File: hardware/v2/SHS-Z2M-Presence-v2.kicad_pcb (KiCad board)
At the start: 2 copper layers, 100 x 70 mm, 36 parts, among them J1 USB_C_Receptacle, SW1 RESET, SW2 BOOT, U1 ESP32-C6-WROOM-1-N8, U2 LD2410C, U3 LD2450, U4 AP2112K-3.3

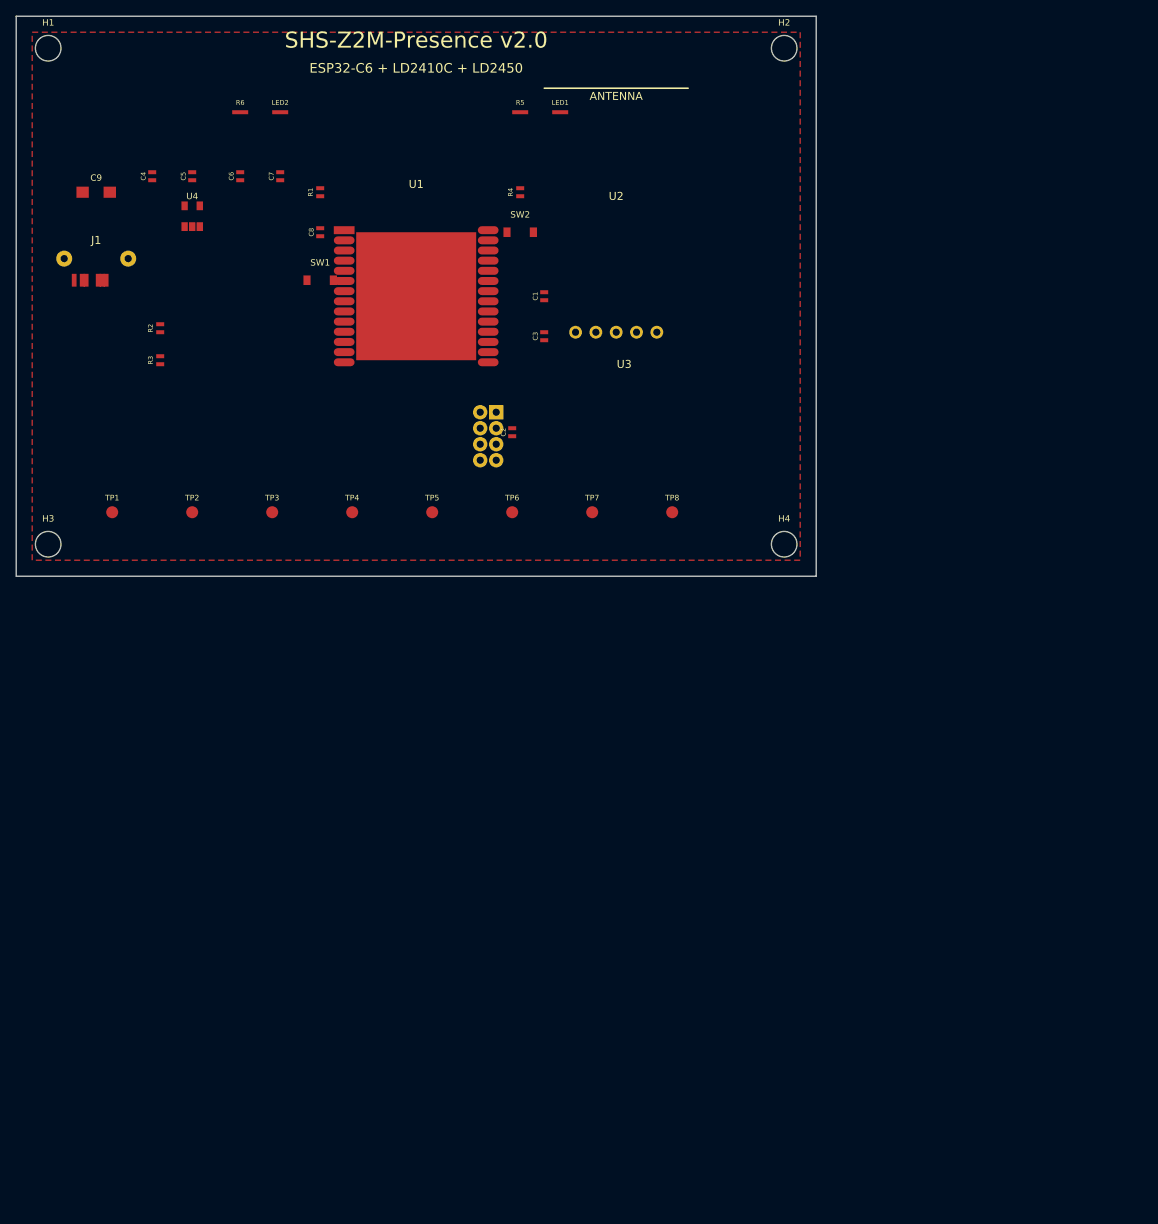
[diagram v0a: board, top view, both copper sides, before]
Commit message: Rewrite v2 PCB layout: compact 39x49mm 4-layer board
- Board outline reduced from 100x70mm to 39x49mm (73% area reduction)
- 4-layer stackup: F.Cu (sensors), In1.Cu (GND plane), In2.Cu (+3V3), B.Cu (SMD)
- Sensors (LD2410C, LD2450) placed on F.Cu with THT headers
- All SMD components (ESP32, LDO, USB-C, passives) on B.Cu
- GND zones on F.Cu, In1.Cu, B.Cu; +3V3 power plane on In2.Cu
- Fiducials at 3 corners for SMD assembly
- Update DESIGN-NOTES.md with 4-layer decision and board dimensions
- Add .history/ to .gitignore (KiCad local undo history)

Co-Authored-By: Claude Opus 4.6 <noreply@anthropic.com>
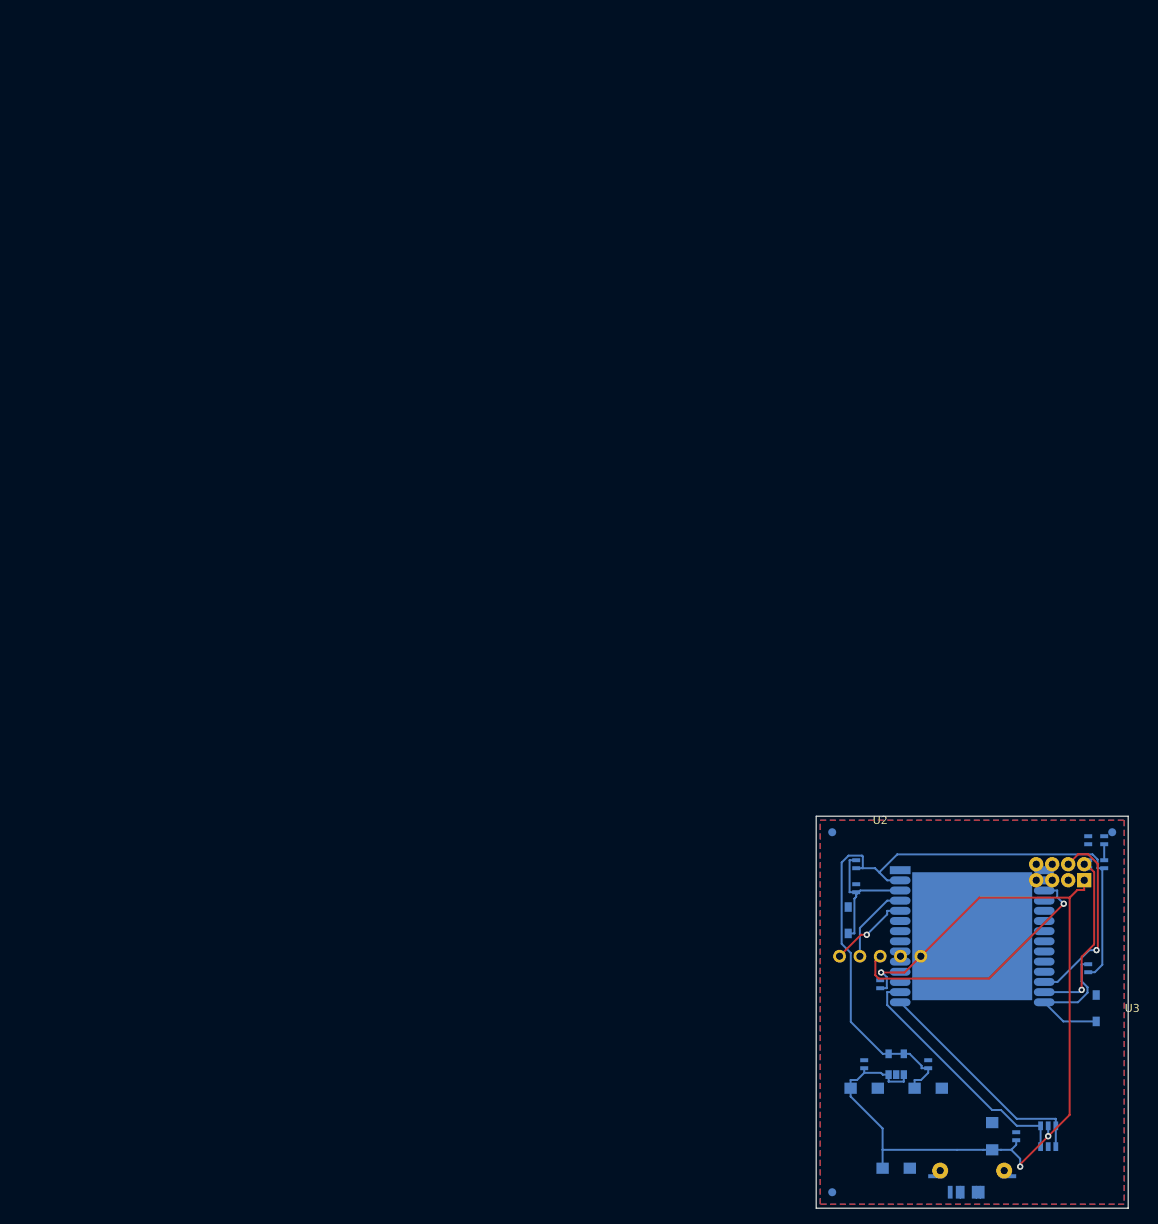
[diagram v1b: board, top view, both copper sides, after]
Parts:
- removed H1, H2, H3, H4: M3, MountingHole:MountingHole_3.2mm_M3
- removed TP1: +5V, TestPoint:TestPoint_Pad_D1.5mm
- removed TP2: +3V3, TestPoint:TestPoint_Pad_D1.5mm
- removed TP3: GND, TestPoint:TestPoint_Pad_D1.5mm
- removed TP4: UART1_TX, TestPoint:TestPoint_Pad_D1.5mm
- removed TP5: UART1_RX, TestPoint:TestPoint_Pad_D1.5mm
- removed TP6: UART0_TX, TestPoint:TestPoint_Pad_D1.5mm
- removed TP7: UART0_RX, TestPoint:TestPoint_Pad_D1.5mm
- removed TP8: ESP_EN, TestPoint:TestPoint_Pad_D1.5mm
- added FID1: Fiducial, Fiducial:Fiducial_1mm_Dia_2mm_Outer, B.Cu at (102.0, 102.0)
- added FID2: Fiducial, Fiducial:Fiducial_1mm_Dia_2mm_Outer, B.Cu at (137.0, 102.0)
- added FID3: Fiducial, Fiducial:Fiducial_1mm_Dia_2mm_Outer, B.Cu at (102.0, 147.0)
- added U5: USBLC6-2SC6, Package_TO_SOT_SMD:SOT-23-6, B.Cu at (129.0, 140.0)
- C1, C2, C4, C6, C8, C9, J1, LED1, LED2, R1, R2, R3, R4, R5, R6, SW1, SW2, U1, U4: moved to B.Cu
- C3, C5, C7: footprint Capacitor_SMD:C_0402_1005Metric -> Capacitor_SMD:C_0805_2012Metric; moved to B.Cu
- moved J1 158.1 mm to (119.5, 147.0)
- moved C9 157.7 mm to (110.0, 144.0)
- moved R3 147.1 mm to (124.0, 145.0), turned to 0 degrees
- moved R2 143.7 mm to (115.0, 145.0), turned to 0 degrees
- moved R6 143.2 mm to (136.0, 106.0), turned to 90 degrees
- moved C4 142.3 mm to (106.0, 131.0)
- moved C5 141.6 mm to (106.0, 134.0), turned to 0 degrees
- moved C6 140.4 mm to (114.0, 131.0)
- moved C7 139.8 mm to (114.0, 134.0), turned to 0 degrees
- moved U4 137.8 mm to (110.0, 131.0)
- moved LED2 137.4 mm to (136.0, 103.0), turned to 90 degrees
- moved SW2 120.8 mm to (135.0, 124.0), turned to 90 degrees
- moved R4 120.2 mm to (134.0, 119.0)
- moved R5 117.8 mm to (134.0, 106.0), turned to 90 degrees
- moved C3 114.6 mm to (122.0, 140.0)
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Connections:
- LED1 pad 1: GND -> Net-R5-A
- LED1 pad 2: Net-R5-A -> GND
- LED2 pad 1: GND -> Net-R6-A
- LED2 pad 2: Net-R6-A -> GND
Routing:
- net +5V: track 0.00 -> 113.7 mm, vias 0 -> 3
- net +3V3: track 0.00 -> 91.7 mm
- net RADAR_OUT: track 0.00 -> 33.8 mm, vias 0 -> 1
- net USB_DM: track 0.00 -> 31.3 mm
- net USB_DP: track 0.00 -> 29.0 mm
- net UART0_RX: track 0.00 -> 23.8 mm, vias 0 -> 1
- net UART0_TX: track 0.00 -> 21.8 mm, vias 0 -> 1
- net BOOT: track 0.00 -> 18.1 mm
- net ESP_EN: track 0.00 -> 17.4 mm
- net UART1_RX: track 0.00 -> 10.2 mm, vias 0 -> 1
- net UART1_TX: track 0.00 -> 9.99 mm
- net Net-R6-A: track 0.00 -> 2.00 mm
- added copper zone on In2.Cu, net +3V3
- added copper zone on B.Cu, net GND
- added copper zone on In1.Cu, net GND
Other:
- board size 100 x 70 mm -> 39 x 49 mm
- copper layers 2 -> 4
- board text added: "SHS-Z2M-Presence v2"
- board text removed: "ANTENNA"
- board text removed: "ESP32-C6 + LD2410C + LD2450"
- board text removed: "SHS-Z2M-Presence v2.0"

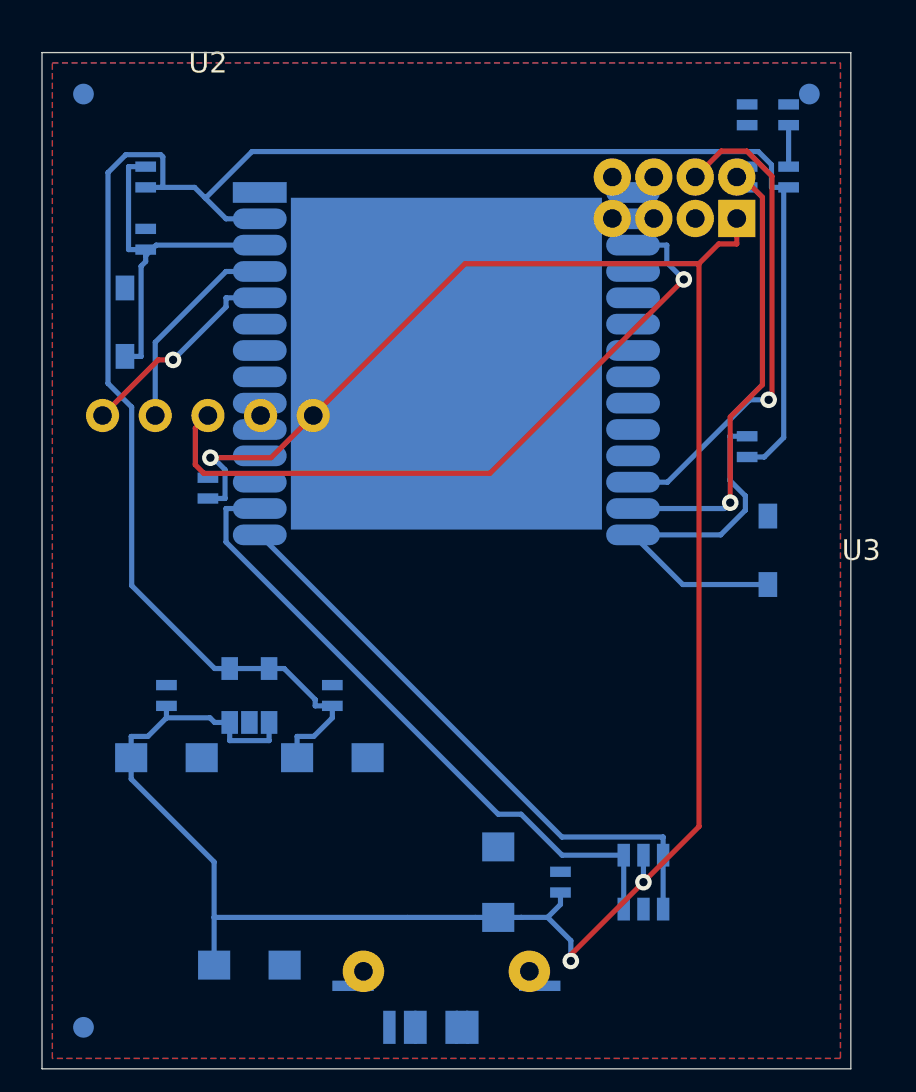
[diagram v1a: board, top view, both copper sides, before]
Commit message: Remove all tracks from v2 PCB for clean rerouting
Strip 134 auto-generated segments — board is now unrouted
and ready for interactive routing in KiCad.

Co-Authored-By: Claude Opus 4.6 <noreply@anthropic.com>
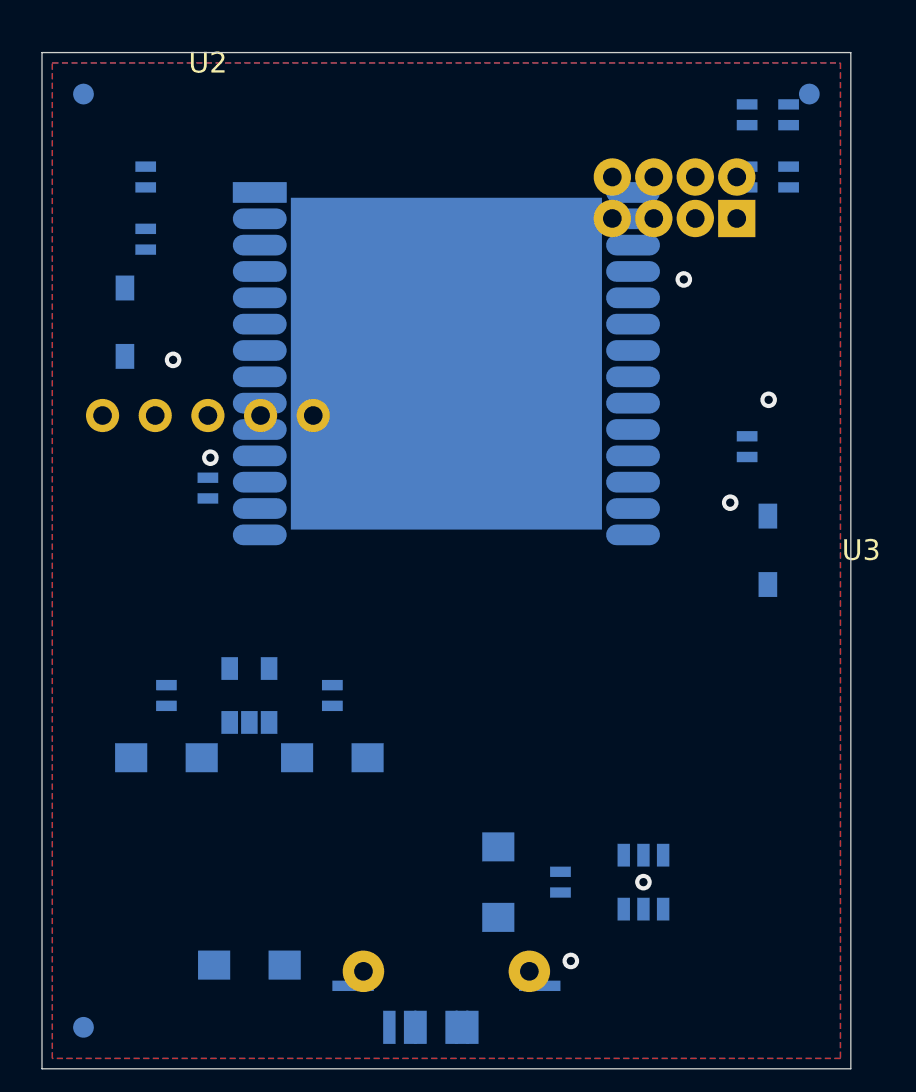
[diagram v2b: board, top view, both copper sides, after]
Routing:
- net +5V: track 113.7 -> 0.00 mm
- net +3V3: track 91.7 -> 0.00 mm
- net RADAR_OUT: track 33.8 -> 0.00 mm
- net USB_DM: track 31.3 -> 0.00 mm
- net USB_DP: track 29.0 -> 0.00 mm
- net UART0_RX: track 23.8 -> 0.00 mm
- net UART0_TX: track 21.8 -> 0.00 mm
- net BOOT: track 18.1 -> 0.00 mm
- net ESP_EN: track 17.4 -> 0.00 mm
- net UART1_RX: track 10.2 -> 0.00 mm
- net UART1_TX: track 9.99 -> 0.00 mm
- net Net-R6-A: track 2.00 -> 0.00 mm
